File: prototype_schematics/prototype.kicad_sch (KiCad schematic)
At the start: 73 parts, among them J1 Conn_Coaxial, J2 Conn_01x03, J3 AudioJack3, U1 MAX2680AUT+, U2 MAX2608EUT+T, U3 SPX3819M5-L-3-3, U4 PSA4-5043, U5 TA0411A, U6 BGA2802, U7 CD74HC4046A, U8 TPA721DR, U9 SPX3819M5-L-3-3, Y1 ECS-96SMF21A30

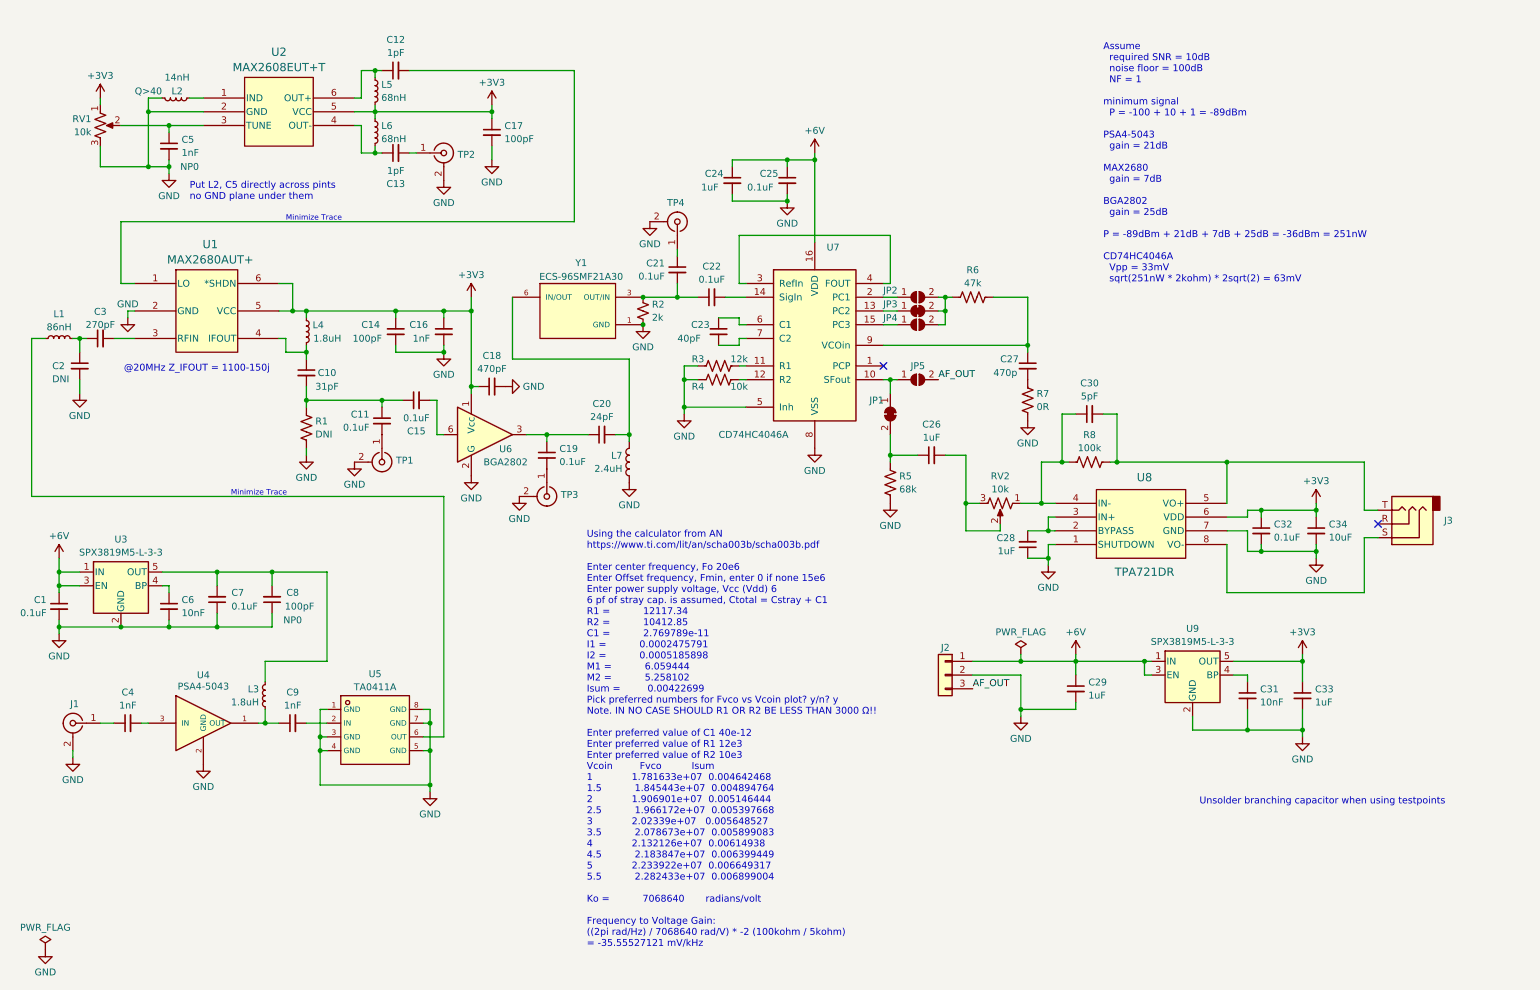
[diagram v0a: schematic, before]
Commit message: add switching regulator to get +6V
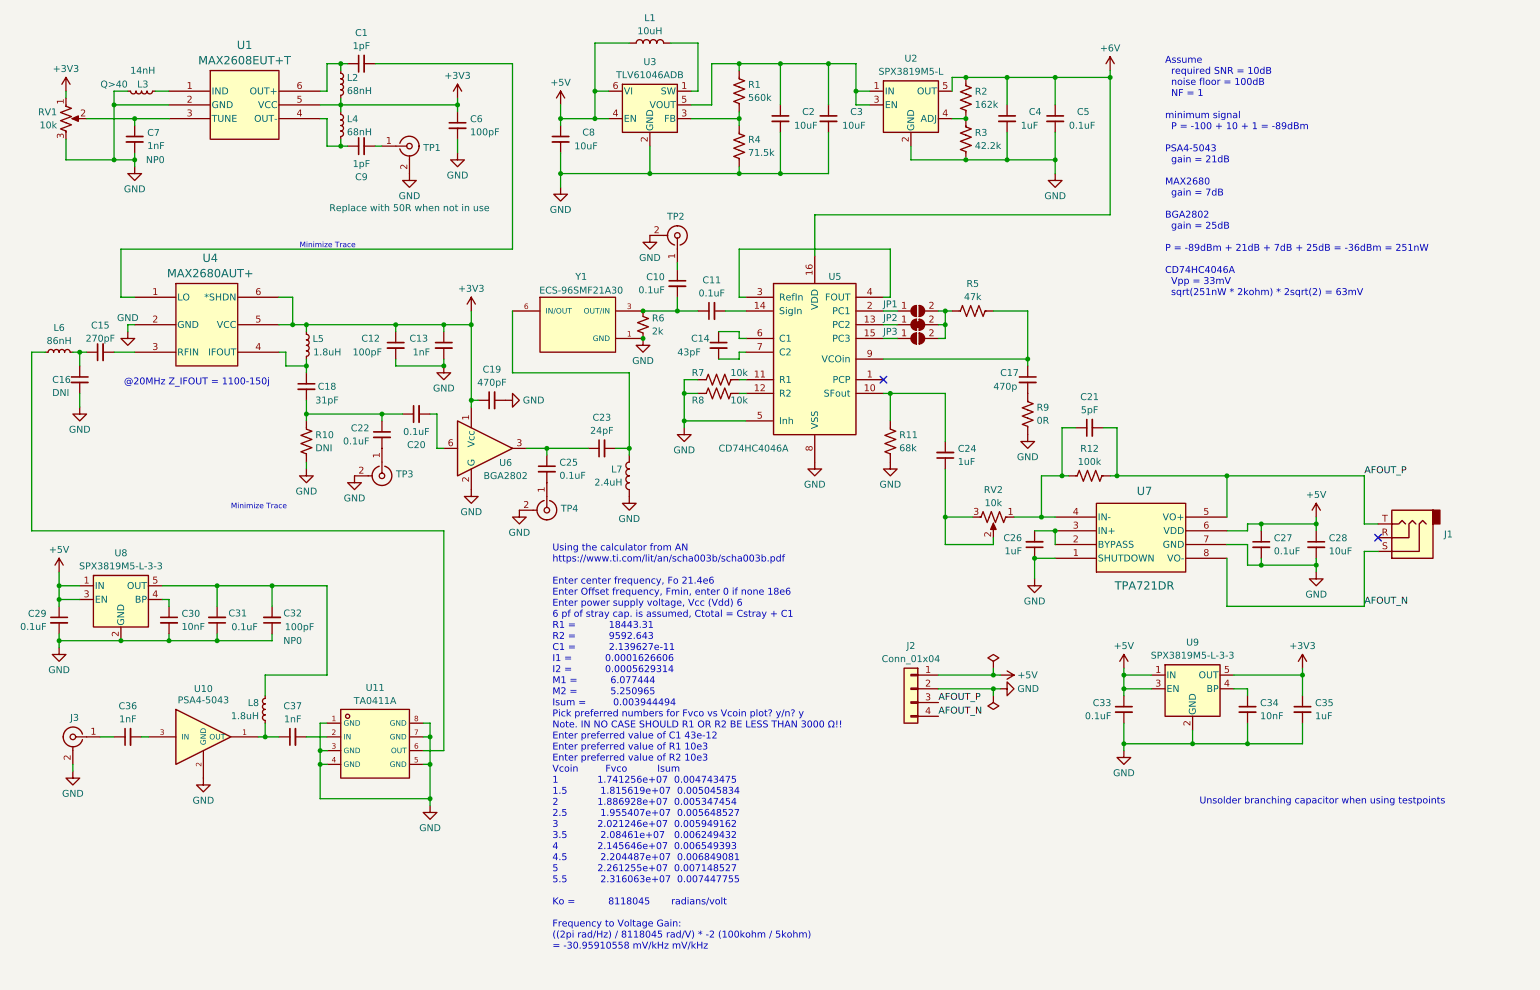
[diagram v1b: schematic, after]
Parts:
- removed C29: 1uF, symbol Device:C_Small
- removed J2: Conn_01x03, symbol Connector_Generic:Conn_01x03
- removed JP1: SolderJumper_2_Bridged, symbol Jumper:SolderJumper_2_Bridged
- removed JP5: SolderJumper_2_Open, symbol Jumper:SolderJumper_2_Open
- added C2, C3, C8: 10uF, symbol Device:C_Small
- added C33: 0.1uF, symbol Device:C_Small
- added J2: Conn_01x04, symbol Connector_Generic:Conn_01x04
- added L1: 10uH, symbol Device:L
- added R1: 560k, symbol Device:R_US
- added R2: 162k, symbol Device:R_US
- added R3: 42.2k, symbol Device:R_US
- added R4: 71.5k, symbol Device:R_US
- added U2: SPX3819M5-L, Package_TO_SOT_SMD:SOT-23-5, symbol Regulator_Linear:SPX3819M5-L
- added U3: TLV61046ADB, Package_TO_SOT_SMD:SOT-23-6, symbol Regulator_Switching:TLV61046ADB
- C14: renamed from C23; value 40pF -> 43pF
- R7: renamed from R3; value 12k -> 10k
- TP1: renamed from TP2; Note (none) -> Replace with 50R when not in use
- U10: renamed from U4; symbol PSA4-5043_:PSA4-5043 -> PSA4-5043:PSA4-5043
- renumbered C12 to C1, C21 to C10, C22 to C11, C14 to C12, C16 to C13, C3 to C15, C2 to C16, C27 to C17, C10 to C18, C18 to C19, C15 to C20, C30 to C21, C11 to C22, C20 to C23, C26 to C24, C19 to C25, C28 to C26, C32 to C27, C34 to C28, C1 to C29, C6 to C30, C7 to C31, C8 to C32, C31 to C34, C33 to C35, C4 to C36, C9 to C37, C24 to C4, C25 to C5, C17 to C6, C5 to C7, C13 to C9, J3 to J1, J1 to J3, JP2 to JP1, JP3 to JP2, JP4 to JP3, L5 to L2, L2 to L3, L6 to L4, L4 to L5, L1 to L6, L3 to L8, R1 to R10, R5 to R11, R8 to R12, R6 to R5, R2 to R6, R4 to R8, R7 to R9, TP4 to TP2, TP1 to TP3, TP3 to TP4, U2 to U1, U5 to U11, U1 to U4, U7 to U5, U8 to U7, U3 to U8
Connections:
- net +3V3: no longer C27.1, C28.1, U7.6 (VDD)
- net +6V: now also R2.1, U2.5 (OUT); no longer C29.1, U8.1 (IN), U8.3 (EN), U9.1 (IN), U9.3 (EN)
- net GND: now also C2.2, C3.2, C33.2, C8.2, J2.2 (Pin_2), R3.2, R4.2, U2.2 (GND), U3.2 (GND)
- net at U5.10 (SFout): now also C24.2, R11.1
- net at C24.1: now also RV2.2, RV2.3; no longer R11.1
- net AFOUT_P: now reaches C21.2, J1.T, R12.2, U7.5 (VO+)
- net AFOUT_P: now also J2.3 (Pin_3)
- net AFOUT_N: now reaches J1.S, U7.8 (VO-)
- net AFOUT_N: now also J2.4 (Pin_4)
- new net: R2.2, R3.1, U2.4 (ADJ)
- new net: C2.1, C3.1, R1.1, U2.1 (IN), U2.3 (EN), U3.5 (VOUT)
- new net: R1.2, R4.1, U3.3 (FB)
- new net: L1.2, U3.1 (SW)
- new net +5V: C27.1, C28.1, C29.1, C33.1, C8.1, J2.1 (Pin_1), L1.1, U3.4 (EN), U3.6 (VI), U7.6 (VDD), U8.1 (IN), U8.3 (EN), U9.1 (IN), U9.3 (EN)
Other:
- note removed: "Put L2, C5 directly across pints no GND plane under them"
- moved on the sheet: C1, C10, C11, C12, C13, C14, C15, C16, C17, C18, C19, C20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

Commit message: add more testpoint
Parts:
- added C38, C39: 1nF, symbol Device:C_Small
- added TP5, TP6: Conn_Coaxial, symbol Connector:Conn_Coaxial
- renumbered C14 to C12, C15 to C13, C12 to C14, C13 to C15
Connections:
- net GND: now also TP5.2 (Ext), TP6.2 (Ext)
- net at L6.1, U11.6 (OUT): now also C39.1
- net at C37.1, L8.2, U10.1 (OUT): now also C38.2
- new net: C38.1, TP5.1 (In)
- new net: C39.2, TP6.1 (In)
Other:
- moved on the sheet: C1, C14, C15, C37, C6, C9, TP1, U11

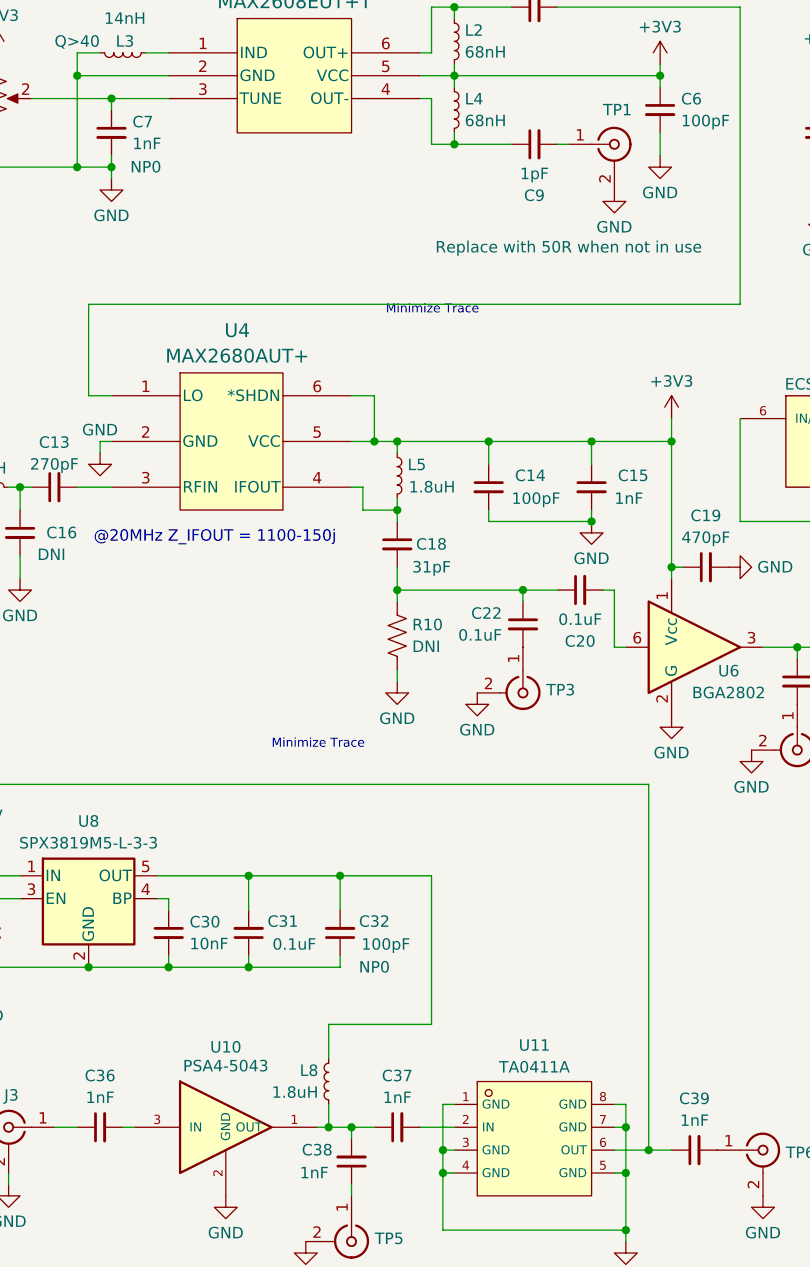
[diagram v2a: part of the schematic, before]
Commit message: update some cap and inductor values
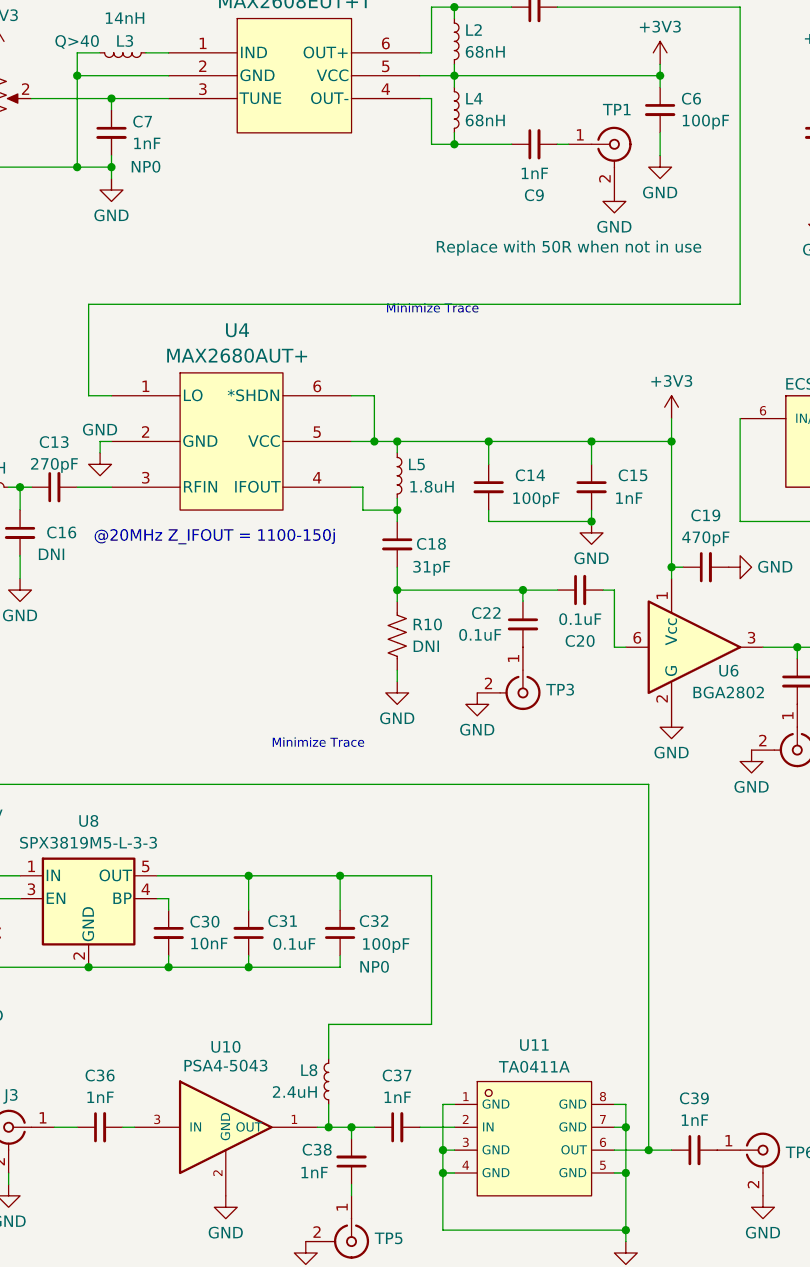
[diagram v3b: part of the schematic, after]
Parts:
- C9: value 1pF -> 1nF
- L8: value 1.8uH -> 2.4uH
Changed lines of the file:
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@@
       (effects (font (size 1.27 1.27)))
     )
-    (property "Value" "1pF" (at 82.5563 46.4622 90)
+    (property "Value" "1nF" (at 82.5563 46.4622 90)
       (effects (font (size 1.27 1.27)))
     )
@@
       (effects (font (size 1.27 1.27)) (justify left))
     )
-    (property "Value" "1.8uH" (at 58.5492 148.5321 0)
-      (effects (font (size 1.27 1.27)) (justify left))
-    )
+    (property "Value" "2.4uH" (at 58.5492 148.5321 0)
+      (effects (font (size 1.27 1.27)) (justify left))
+    )

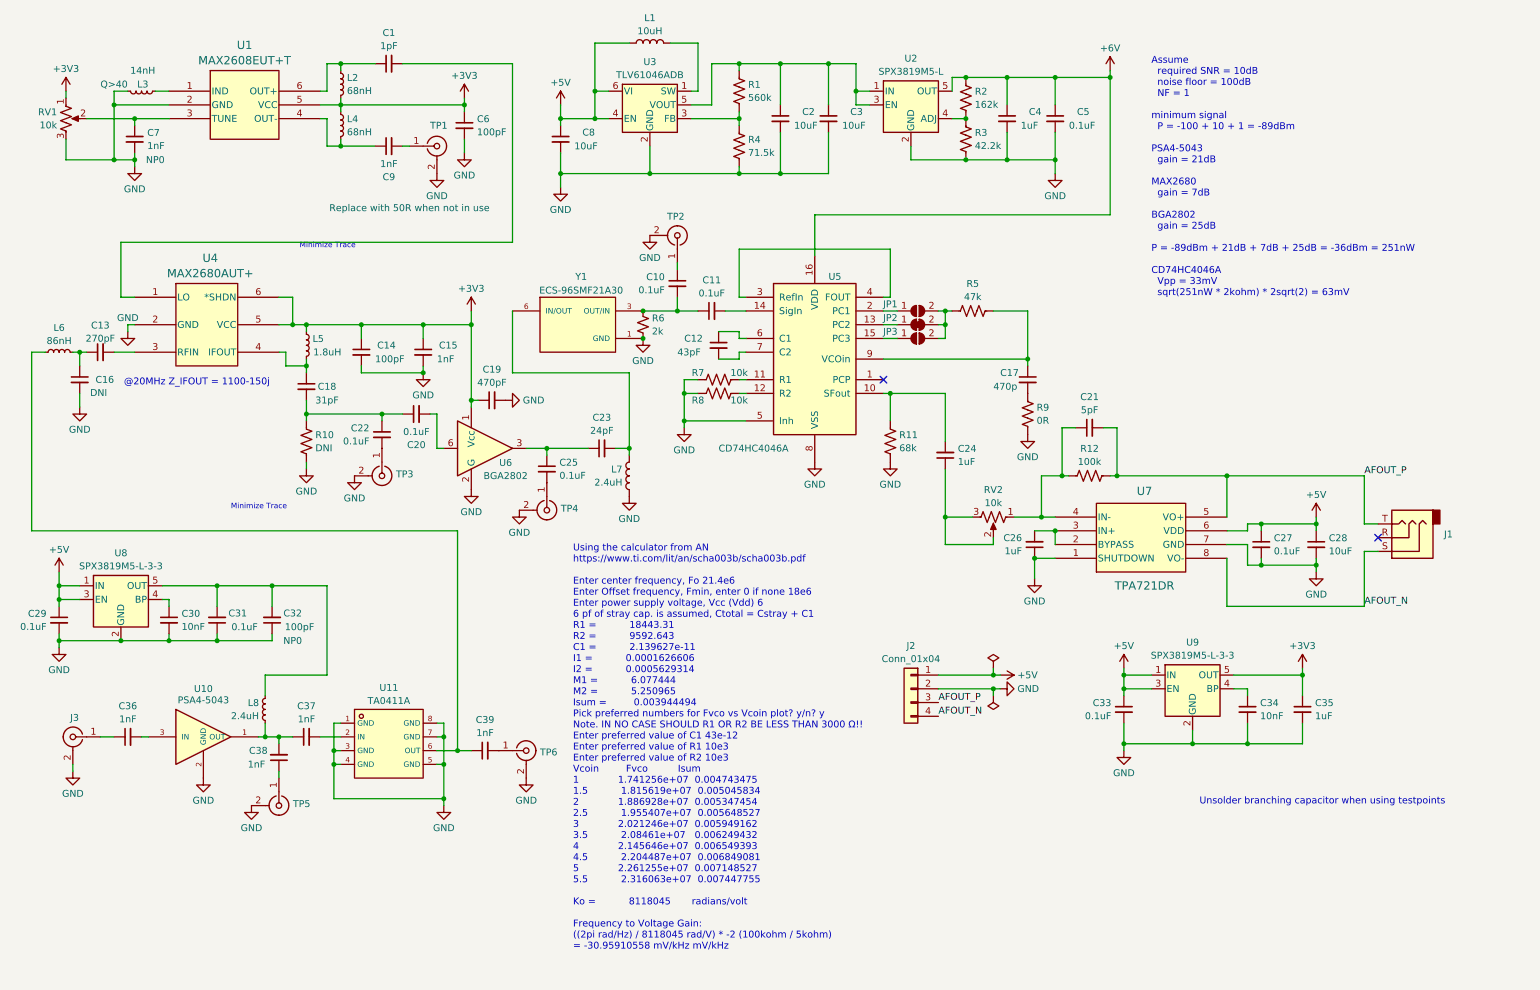
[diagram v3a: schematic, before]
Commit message: fix testpoint impedance matching; remove dedicated LDO
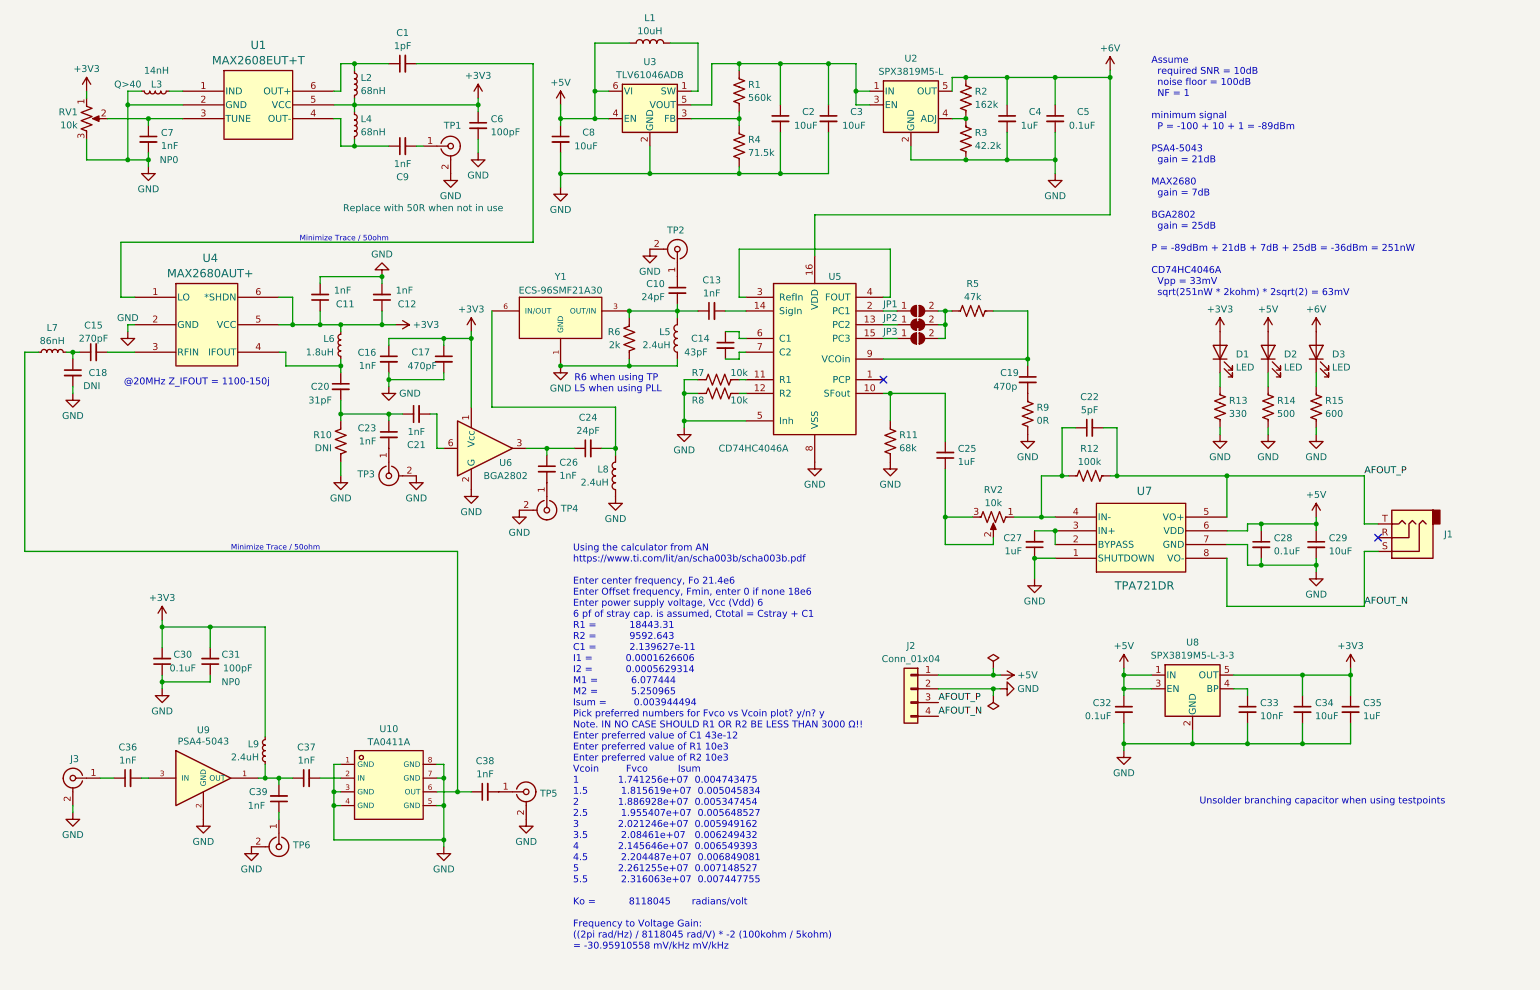
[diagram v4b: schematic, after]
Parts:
- removed C19: 470pF, symbol Device:C_Small
- removed C29: 0.1uF, symbol Device:C_Small
- removed C30: 10nF, symbol Device:C_Small
- removed R6: 2k, symbol Device:R_Small_US
- removed U8: SPX3819M5-L-3-3, Package_TO_SOT_SMD:SOT-23-5, symbol Regulator_Linear:SPX3819M5-L-3-3
- added C16: 1nF, symbol Device:C_Small
- added C17: 470pF, symbol Device:C_Small
- added C34: 10uF, symbol Device:C_Small
- added D1, D2, D3: LED, symbol Device:LED
- added L5: 2.4uH, symbol Device:L
- added R13: 330, symbol Device:R_US
- added R14: 500, symbol Device:R_US
- added R15: 600, symbol Device:R_US
- added R6: 2k, symbol Device:R_US
- C10: value 0.1uF -> 24pF
- C11: renamed from C14; value 100pF -> 1nF
- C13: renamed from C11; value 0.1uF -> 1nF
- C21: renamed from C20; value 0.1uF -> 1nF
- C23: renamed from C22; value 0.1uF -> 1nF
- C26: renamed from C25; value 0.1uF -> 1nF
- renumbered C15 to C12, C12 to C14, C13 to C15, C16 to C18, C17 to C19, C18 to C20, C21 to C22, C23 to C24, C24 to C25, C26 to C27, C27 to C28, C28 to C29, C31 to C30, C32 to C31, C33 to C32, C34 to C33, C39 to C38, C38 to C39, L5 to L6, L6 to L7, L7 to L8, L8 to L9, TP6 to TP5, TP5 to TP6, U11 to U10, U9 to U8, U10 to U9
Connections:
- net +3V3: now also C30.2, C31.2, L9.1, C16.1, C17.1, C34.1, D1.2 (A)
- net +5V: now also D2.2 (A)
- net +6V: now also D3.2 (A)
- net GND: now also C16.2, C17.2, C34.2, L5.2, R13.2, R14.2, R15.2, R6.2
- net at C10.2, C13.1, Y1.3 (OUT/IN): now also L5.1, R6.1
- new net: D2.1 (K), R14.1
- new net: D3.1 (K), R15.1
- new net: D1.1 (K), R13.1
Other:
- note added: "Minimize Trace / 50ohm"
- note added: "R6 when using TP L5 when using PLL"
- note removed: "Minimize Trace"
- moved on the sheet: C1, C11, C12, C14, C15, C18, C20, C23, C24, C30, C31, C35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
